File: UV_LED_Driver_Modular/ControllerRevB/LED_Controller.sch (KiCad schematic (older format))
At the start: 11 parts, among them J1 Barrel_Jack, J2 Conn_01x05, J4 Conn_02x04_Odd_Even, SW1 SW_SPST, SW3 SW_SPST, U1 STM32F051K8Tx, U2 L78L33_SOT89

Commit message: hw update
controller revb
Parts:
- added BZ1: Buzzer, Connector_PinHeader_2.54mm:PinHeader_1x02_P2.54mm_Vertical, symbol Device:Buzzer
- added D1: D, Diode_SMD:D_SOD-123F, symbol Device:D
- added Q1: MMBT3904, Package_TO_SOT_SMD:SOT-23, symbol Transistor_BJT:MMBT3904
- added SW4: SW_SPST, Connector_PinHeader_2.54mm:PinHeader_1x02_P2.54mm_Vertical, symbol Switch:SW_SPST
- added U3: MCP1416, Package_TO_SOT_SMD:SOT-23-5, symbol Driver_FET:MCP1416
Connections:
- net 3V3: now also SW4.1 (A)
- net GNDS: now also Q1.2 (E), U3.4 (GND)
- net VPP: now also BZ1.1 (-), D1.1 (K), U3.2 (Vdd)
- net BUZZER_PWM: now reaches U1.27 (PB4)
- net BUZZER_PWM: now also U3.3 (IN)
- net DOWN_BTN: now reaches U1.7 (PA1)
- net DOWN_BTN: now also SW4.2 (B)
- net MINUTE_BTN renamed UP_BTN
- new net: BZ1.2 (+), D1.2 (A), Q1.3 (C)
- new net: Q1.1 (B), U3.5 (OUT)
- no-connect marks 9 -> 7
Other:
- moved on the sheet: SW3
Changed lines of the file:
@@
 	-1   0    0    -1
 $EndComp
-Text Label 5325 2625 0    50   ~ 0
+Text Label 5200 2625 0    50   ~ 0
 NRST
 Wire Wire Line
-	5775 2625 5325 2625
+	5775 2625 5200 2625
 Wire Wire Line
 	4625 2825 4625 2975
@@
 	6475 2325 6475 2425
 Connection ~ 6375 2325
-Text Label 5275 3225 0    50   ~ 0
+Text Label 5175 3225 0    50   ~ 0
 ENABLE_LED
 Wire Wire Line
-	5275 3225 5775 3225
+	5175 3225 5775 3225
 Text Label 7625 3725 2    50   ~ 0
 LED_CTRL1
@@
 NoConn ~ 5775 4025
 NoConn ~ 5775 3925
-NoConn ~ 5775 3825
 NoConn ~ 5775 3325
 Text HLabel 9850 3250 2    50   Input ~ 0
@@
 	3150 5375 2650 5375
 Wire Wire Line
-	5775 3625 5275 3625
-Text Label 5275 3625 0    50   ~ 0
+	5775 3625 5175 3625
+Text Label 5175 3625 0    50   ~ 0
 LED_CTRL5
 Wire Wire Line
@@
 	6875 4125 7375 4125
 Wire Wire Line
-	5775 3725 5275 3725
-Text Label 5275 3725 0    50   ~ 0
+	5775 3725 5175 3725
+Text Label 5175 3725 0    50   ~ 0
 ENC_A
 Text Label 7375 4125 2    50   ~ 0
@@
 TFT_MOSI
 Wire Wire Line
-	5775 3525 5275 3525
-Text Label 5275 3525 0    50   ~ 0
+	5775 3525 5175 3525
+Text Label 5175 3525 0    50   ~ 0
 TFT_RST
 Wire Wire Line
@@
 Wire Wire Line
 	9800 1975 10250 1975
-NoConn ~ 6875 2725
 Text Label 8825 1975 0    50   ~ 0
 TFT_LED
@@
 L Switch:SW_SPST SW3
 U 1 1 5EFC8DE0
-P 2475 4150
-F 0 "SW3" H 2475 4385 50  0000 C CNN
-F 1 "SW_SPST" H 2475 4294 50  0000 C CNN
-F 2 "Connector_PinHeader_2.54mm:PinHeader_1x02_P2.54mm_Vertical" H 2475 4150 50  0001 C CNN
-F 3 "~" H 2475 4150 50  0001 C CNN
-	1    2475 4150
-	1    0    0    -1
-$EndComp
-Text Label 3175 4150 2    50   ~ 0
-MINUTE_BTN
-Wire Wire Line
-	3175 4150 2675 4150
+P 2450 3875
+F 0 "SW3" H 2450 4110 50  0000 C CNN
+F 1 "SW_SPST" H 2450 4019 50  0000 C CNN
+F 2 "Connector_PinHeader_2.54mm:PinHeader_1x02_P2.54mm_Vertical" H 2450 3875 50  0001 C CNN
+F 3 "~" H 2450 3875 50  0001 C CNN
+	1    2450 3875
+	1    0    0    -1
+$EndComp
+Text Label 3150 3875 2    50   ~ 0
+UP_BTN
+Wire Wire Line
+	3150 3875 2650 3875
 Text Label 7625 2825 2    50   ~ 0
-MINUTE_BTN
+UP_BTN
 Wire Wire Line
 	7625 2825 6875 2825
 Wire Wire Line
-	1875 4150 1875 3825
-Text HLabel 1875 3825 1    50   Input ~ 0
-3V3
-Wire Wire Line
-	1875 4150 2275 4150
+	1850 3875 1850 3550
+Text HLabel 1850 3550 1    50   Input ~ 0
+3V3
+Wire Wire Line
+	1850 3875 2250 3875
 Wire Wire Line
 	1850 5375 1850 5050
@@
 Text HLabel 10250 1975 2    50   Input ~ 0
 VPP
+$Comp
+L Device:Buzzer BZ1
+U 1 1 5EF2925A
+P 9400 4875
+F 0 "BZ1" H 9552 4904 50  0000 L CNN
+F 1 "Buzzer" H 9552 4813 50  0000 L CNN
+F 2 "Connector_PinHeader_2.54mm:PinHeader_1x02_P2.54mm_Vertical" V 9375 4975 50  0001 C CNN
+F 3 "~" V 9375 4975 50  0001 C CNN
+	1    9400 4875
+	1    0    0    -1
+$EndComp
+$Comp
+L Driver_FET:MCP1416 U3
+U 1 1 5EF2A524
+P 8200 5425
+F 0 "U3" H 7750 5825 50  0000 L CNN
+F 1 "MCP1416" H 7700 5725 50  0000 L CNN
+F 2 "Package_TO_SOT_SMD:SOT-23-5" H 8200 5025 50  0001 C CIN
+F 3 "http://ww1.microchip.com/downloads/en/DeviceDoc/20002092F.pdf" H 8000 5675 50  0001 C CNN
+	1    8200 5425
+	1    0    0    -1
+$EndComp
+$Comp
+L Transistor_BJT:MMBT3904 Q1
+U 1 1 5EF2B431
+P 9200 5425
+F 0 "Q1" H 9391 5471 50  0000 L CNN
+F 1 "MMBT3904" H 9391 5380 50  0000 L CNN
+F 2 "Package_TO_SOT_SMD:SOT-23" H 9400 5350 50  0001 L CIN
+F 3 "https://www.fairchildsemi.com/datasheets/2N/2N3904.pdf" H 9200 5425 50  0001 L CNN
+	1    9200 5425
+	1    0    0    -1
+$EndComp
+Text HLabel 8200 5000 1    50   Input ~ 0
+VPP
+Wire Wire Line
+	8200 5000 8200 5125
+$Comp
+L power:GNDS #PWR05
+U 1 1 5EF3198B
+P 8200 5925
+F 0 "#PWR05" H 8200 5675 50  0001 C CNN
+F 1 "GNDS" H 8205 5752 50  0000 C CNN
+F 2 "" H 8200 5925 50  0001 C CNN
+F 3 "" H 8200 5925 50  0001 C CNN
+	1    8200 5925
+	-1   0    0    -1
+$EndComp
+Wire Wire Line
+	8200 5925 8200 5725
+Wire Wire Line
+	8600 5425 9000 5425
+Text HLabel 9300 4400 1    50   Input ~ 0
+VPP
+Wire Wire Line
+	9300 4400 9300 4600
+$Comp
+L power:GNDS #PWR06
+U 1 1 5EF46BCB
+P 9300 5925
+F 0 "#PWR06" H 9300 5675 50  0001 C CNN
+F 1 "GNDS" H 9305 5752 50  0000 C CNN
+F 2 "" H 9300 5925 50  0001 C CNN
+F 3 "" H 9300 5925 50  0001 C CNN
+	1    9300 5925
+	-1   0    0    -1
+$EndComp
+Wire Wire Line
+	9300 5925 9300 5625
+Wire Wire Line
+	9300 4975 9300 5150
+$Comp
+L Device:D D1
+U 1 1 5EF4FFE8
+P 9000 4875
+F 0 "D1" V 8950 4725 50  0000 L CNN
+F 1 "D" V 9050 4725 50  0000 L CNN
+F 2 "Diode_SMD:D_SOD-123F" H 9000 4875 50  0001 C CNN
+F 3 "~" H 9000 4875 50  0001 C CNN
+	1    9000 4875
+	0    1    1    0
+$EndComp
+Wire Wire Line
+	9000 4725 9000 4600
+Wire Wire Line
+	9000 4600 9300 4600
+Connection ~ 9300 4600
+Wire Wire Line
+	9300 4600 9300 4775
+Wire Wire Line
+	9000 5025 9000 5150
+Wire Wire Line
+	9000 5150 9300 5150
+Connection ~ 9300 5150
+Wire Wire Line
+	9300 5150 9300 5225
+Wire Wire Line
+	5775 3825 5175 3825
+Text Label 5175 3825 0    50   ~ 0
+BUZZER_PWM
+Text Label 7250 5425 0    50   ~ 0
+BUZZER_PWM
+Wire Wire Line
+	7250 5425 7900 5425
+$Comp
+L Switch:SW_SPST SW4
+U 1 1 5EF795B5
+P 2450 4550
+F 0 "SW4" H 2450 4785 50  0000 C CNN
+F 1 "SW_SPST" H 2450 4694 50  0000 C CNN
+F 2 "Connector_PinHeader_2.54mm:PinHeader_1x02_P2.54mm_Vertical" H 2450 4550 50  0001 C CNN
+F 3 "~" H 2450 4550 50  0001 C CNN
+	1    2450 4550
+	1    0    0    -1
+$EndComp
+Text Label 3150 4550 2    50   ~ 0
+DOWN_BTN
+Wire Wire Line
+	3150 4550 2650 4550
+Wire Wire Line
+	1850 4550 1850 4225
+Text HLabel 1850 4225 1    50   Input ~ 0
+3V3
+Wire Wire Line
+	1850 4550 2250 4550
+Text Label 7625 2725 2    50   ~ 0
+DOWN_BTN
+Wire Wire Line
+	7625 2725 6875 2725
 $EndSCHEMATC

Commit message: updated
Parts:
- J1: footprint Connector_Molex:Molex_KK-396_A-41791-0002_1x02_P3.96mm_Vertical -> Connector_Molex:Molex_KK-254_AE-6410-02A_1x02_P2.54mm_Vertical
- R1: value 10K -> 1K
- R4: value 0R -> 1K
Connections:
- net 3V3: no longer R1.1
- net BUZZER_PWM: now also R1.2; no longer U3.3 (IN)
- net GNDS: now also U1.31 (BOOT0); no longer R4.2
- net at U3.5 (OUT): now also R4.2; no longer Q1.1 (B)
- new net: R1.1, U3.3 (IN)
- new net: Q1.1 (B), R4.1
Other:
- moved on the sheet: BZ1, D1, Q1, U3
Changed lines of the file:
@@
 Wire Wire Line
 	5775 2625 5200 2625
-Wire Wire Line
-	4625 2825 4625 2975
 $Comp
 L power:GNDS #PWR021
@@
 F 0 "J1" H 1682 1775 50  0000 C CNN
 F 1 "Barrel_Jack" H 1682 1684 50  0000 C CNN
-F 2 "Connector_Molex:Molex_KK-396_A-41791-0002_1x02_P3.96mm_Vertical" H 1675 1410 50  0001 C CNN
+F 2 "Connector_Molex:Molex_KK-254_AE-6410-02A_1x02_P2.54mm_Vertical" H 1675 1410 50  0001 C CNN
 F 3 "~" H 1675 1410 50  0001 C CNN
 	1    1625 1450
@@
 Wire Wire Line
 	9300 1875 8825 1875
-$Comp
-L Device:R R1
-U 1 1 5EF88471
-P 4625 2425
-F 0 "R1" H 4695 2471 50  0000 L CNN
-F 1 "10K" H 4695 2380 50  0000 L CNN
-F 2 "Resistor_SMD:R_1206_3216Metric_Pad1.42x1.75mm_HandSolder" V 4555 2425 50  0001 C CNN
-F 3 "~" H 4625 2425 50  0001 C CNN
-	1    4625 2425
-	1    0    0    -1
-$EndComp
-Wire Wire Line
-	4625 2575 4625 2825
-Connection ~ 4625 2825
-$Comp
-L Device:R R4
-U 1 1 5EF8AB44
-P 4625 3125
-F 0 "R4" H 4695 3171 50  0000 L CNN
-F 1 "0R" H 4695 3080 50  0000 L CNN
-F 2 "Resistor_SMD:R_1206_3216Metric_Pad1.42x1.75mm_HandSolder" V 4555 3125 50  0001 C CNN
-F 3 "~" H 4625 3125 50  0001 C CNN
-	1    4625 3125
-	1    0    0    -1
-$EndComp
-Wire Wire Line
-	4625 3275 4625 3500
 Wire Wire Line
 	4625 2825 5775 2825
-Wire Wire Line
-	4625 2275 4625 1800
-Text HLabel 4625 1800 1    50   Input ~ 0
-3V3
 $Comp
 L Switch:SW_SPST SW3
@@
 L Device:Buzzer BZ1
 U 1 1 5EF2925A
-P 9400 4875
-F 0 "BZ1" H 9552 4904 50  0000 L CNN
-F 1 "Buzzer" H 9552 4813 50  0000 L CNN
-F 2 "Connector_PinHeader_2.54mm:PinHeader_1x02_P2.54mm_Vertical" V 9375 4975 50  0001 C CNN
-F 3 "~" V 9375 4975 50  0001 C CNN
-	1    9400 4875
+P 10300 4750
+F 0 "BZ1" H 10452 4779 50  0000 L CNN
+F 1 "Buzzer" H 10452 4688 50  0000 L CNN
+F 2 "Connector_PinHeader_2.54mm:PinHeader_1x02_P2.54mm_Vertical" V 10275 4850 50  0001 C CNN
+F 3 "~" V 10275 4850 50  0001 C CNN
+	1    10300 4750
 	1    0    0    -1
 $EndComp
@@
 L Driver_FET:MCP1416 U3
 U 1 1 5EF2A524
-P 8200 5425
-F 0 "U3" H 7750 5825 50  0000 L CNN
-F 1 "MCP1416" H 7700 5725 50  0000 L CNN
-F 2 "Package_TO_SOT_SMD:SOT-23-5" H 8200 5025 50  0001 C CIN
-F 3 "http://ww1.microchip.com/downloads/en/DeviceDoc/20002092F.pdf" H 8000 5675 50  0001 C CNN
-	1    8200 5425
+P 8800 5300
+F 0 "U3" H 8350 5700 50  0000 L CNN
+F 1 "MCP1416" H 8300 5600 50  0000 L CNN
+F 2 "Package_TO_SOT_SMD:SOT-23-5" H 8800 4900 50  0001 C CIN
+F 3 "http://ww1.microchip.com/downloads/en/DeviceDoc/20002092F.pdf" H 8600 5550 50  0001 C CNN
+	1    8800 5300
 	1    0    0    -1
 $EndComp
@@
 L Transistor_BJT:MMBT3904 Q1
 U 1 1 5EF2B431
-P 9200 5425
-F 0 "Q1" H 9391 5471 50  0000 L CNN
-F 1 "MMBT3904" H 9391 5380 50  0000 L CNN
-F 2 "Package_TO_SOT_SMD:SOT-23" H 9400 5350 50  0001 L CIN
-F 3 "https://www.fairchildsemi.com/datasheets/2N/2N3904.pdf" H 9200 5425 50  0001 L CNN
-	1    9200 5425
-	1    0    0    -1
-$EndComp
-Text HLabel 8200 5000 1    50   Input ~ 0
+P 10100 5300
+F 0 "Q1" H 10291 5346 50  0000 L CNN
+F 1 "MMBT3904" H 10291 5255 50  0000 L CNN
+F 2 "Package_TO_SOT_SMD:SOT-23" H 10300 5225 50  0001 L CIN
+F 3 "https://www.fairchildsemi.com/datasheets/2N/2N3904.pdf" H 10100 5300 50  0001 L CNN
+	1    10100 5300
+	1    0    0    -1
+$EndComp
+Text HLabel 8800 4875 1    50   Input ~ 0
 VPP
 Wire Wire Line
-	8200 5000 8200 5125
+	8800 4875 8800 5000
 $Comp
 L power:GNDS #PWR05
 U 1 1 5EF3198B
-P 8200 5925
-F 0 "#PWR05" H 8200 5675 50  0001 C CNN
-F 1 "GNDS" H 8205 5752 50  0000 C CNN
-F 2 "" H 8200 5925 50  0001 C CNN
-F 3 "" H 8200 5925 50  0001 C CNN
-	1    8200 5925
+P 8800 5800
+F 0 "#PWR05" H 8800 5550 50  0001 C CNN
+F 1 "GNDS" H 8805 5627 50  0000 C CNN
+F 2 "" H 8800 5800 50  0001 C CNN
+F 3 "" H 8800 5800 50  0001 C CNN
+	1    8800 5800
 	-1   0    0    -1
 $EndComp
 Wire Wire Line
-	8200 5925 8200 5725
-Wire Wire Line
-	8600 5425 9000 5425
-Text HLabel 9300 4400 1    50   Input ~ 0
+	8800 5800 8800 5600
+Wire Wire Line
+	9200 5300 9425 5300
+Text HLabel 10200 4275 1    50   Input ~ 0
 VPP
 Wire Wire Line
-	9300 4400 9300 4600
+	10200 4275 10200 4475
 $Comp
 L power:GNDS #PWR06
 U 1 1 5EF46BCB
-P 9300 5925
-F 0 "#PWR06" H 9300 5675 50  0001 C CNN
-F 1 "GNDS" H 9305 5752 50  0000 C CNN
-F 2 "" H 9300 5925 50  0001 C CNN
-F 3 "" H 9300 5925 50  0001 C CNN
-	1    9300 5925
+P 10200 5800
+F 0 "#PWR06" H 10200 5550 50  0001 C CNN
+F 1 "GNDS" H 10205 5627 50  0000 C CNN
+F 2 "" H 10200 5800 50  0001 C CNN
+F 3 "" H 10200 5800 50  0001 C CNN
+	1    10200 5800
 	-1   0    0    -1
 $EndComp
 Wire Wire Line
-	9300 5925 9300 5625
-Wire Wire Line
-	9300 4975 9300 5150
+	10200 5800 10200 5500
+Wire Wire Line
+	10200 4850 10200 5025
 $Comp
 L Device:D D1
 U 1 1 5EF4FFE8
-P 9000 4875
-F 0 "D1" V 8950 4725 50  0000 L CNN
-F 1 "D" V 9050 4725 50  0000 L CNN
-F 2 "Diode_SMD:D_SOD-123F" H 9000 4875 50  0001 C CNN
-F 3 "~" H 9000 4875 50  0001 C CNN
-	1    9000 4875
+P 9900 4750
+F 0 "D1" V 9850 4600 50  0000 L CNN
+F 1 "D" V 9950 4600 50  0000 L CNN
+F 2 "Diode_SMD:D_SOD-123F" H 9900 4750 50  0001 C CNN
+F 3 "~" H 9900 4750 50  0001 C CNN
+	1    9900 4750
 	0    1    1    0
 $EndComp
 Wire Wire Line
-	9000 4725 9000 4600
-Wire Wire Line
-	9000 4600 9300 4600
-Connection ~ 9300 4600
-Wire Wire Line
-	9300 4600 9300 4775
-Wire Wire Line
-	9000 5025 9000 5150
-Wire Wire Line
-	9000 5150 9300 5150
-Connection ~ 9300 5150
-Wire Wire Line
-	9300 5150 9300 5225
+	9900 4600 9900 4475
+Wire Wire Line
+	9900 4475 10200 4475
+Connection ~ 10200 4475
+Wire Wire Line
+	10200 4475 10200 4650
+Wire Wire Line
+	9900 4900 9900 5025
+Wire Wire Line
+	9900 5025 10200 5025
+Connection ~ 10200 5025
+Wire Wire Line
+	10200 5025 10200 5100
 Wire Wire Line
 	5775 3825 5175 3825
 Text Label 5175 3825 0    50   ~ 0
 BUZZER_PWM
-Text Label 7250 5425 0    50   ~ 0
+Text Label 7350 5300 0    50   ~ 0
 BUZZER_PWM
 Wire Wire Line
-	7250 5425 7900 5425
+	7350 5300 8000 5300
 $Comp
 L Switch:SW_SPST SW4
@@
 Wire Wire Line
 	7625 2725 6875 2725
+Wire Wire Line
+	4625 2825 4625 3500
+$Comp
+L Device:R R1
+U 1 1 5EF88709
+P 8150 5300
+F 0 "R1" V 7943 5300 50  0000 C CNN
+F 1 "1K" V 8034 5300 50  0000 C CNN
+F 2 "Resistor_SMD:R_1206_3216Metric_Pad1.42x1.75mm_HandSolder" V 8080 5300 50  0001 C CNN
+F 3 "~" H 8150 5300 50  0001 C CNN
+	1    8150 5300
+	0    1    1    0
+$EndComp
+Wire Wire Line
+	8300 5300 8500 5300
+$Comp
+L Device:R R4
+U 1 1 5EF94EF7
+P 9575 5300
+F 0 "R4" V 9368 5300 50  0000 C CNN
+F 1 "1K" V 9459 5300 50  0000 C CNN
+F 2 "Resistor_SMD:R_1206_3216Metric_Pad1.42x1.75mm_HandSolder" V 9505 5300 50  0001 C CNN
+F 3 "~" H 9575 5300 50  0001 C CNN
+	1    9575 5300
+	0    1    1    0
+$EndComp
+Wire Wire Line
+	9725 5300 9900 5300
 $EndSCHEMATC

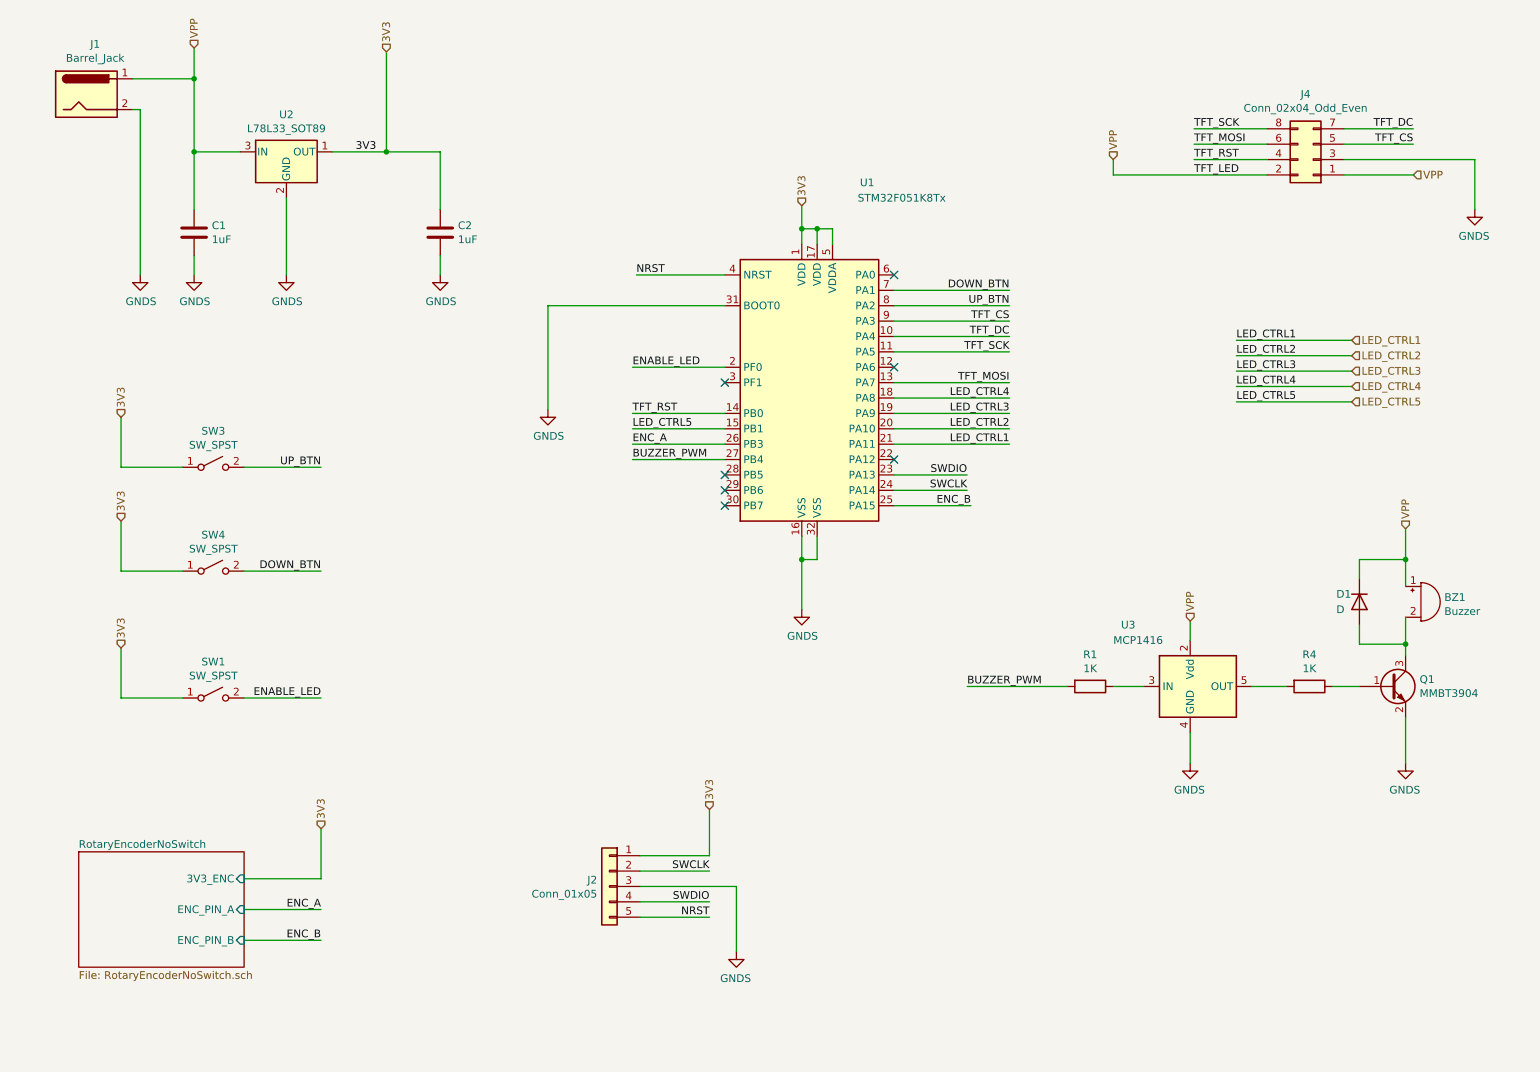
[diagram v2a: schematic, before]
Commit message: Updated prototype designs for fab
updated readme
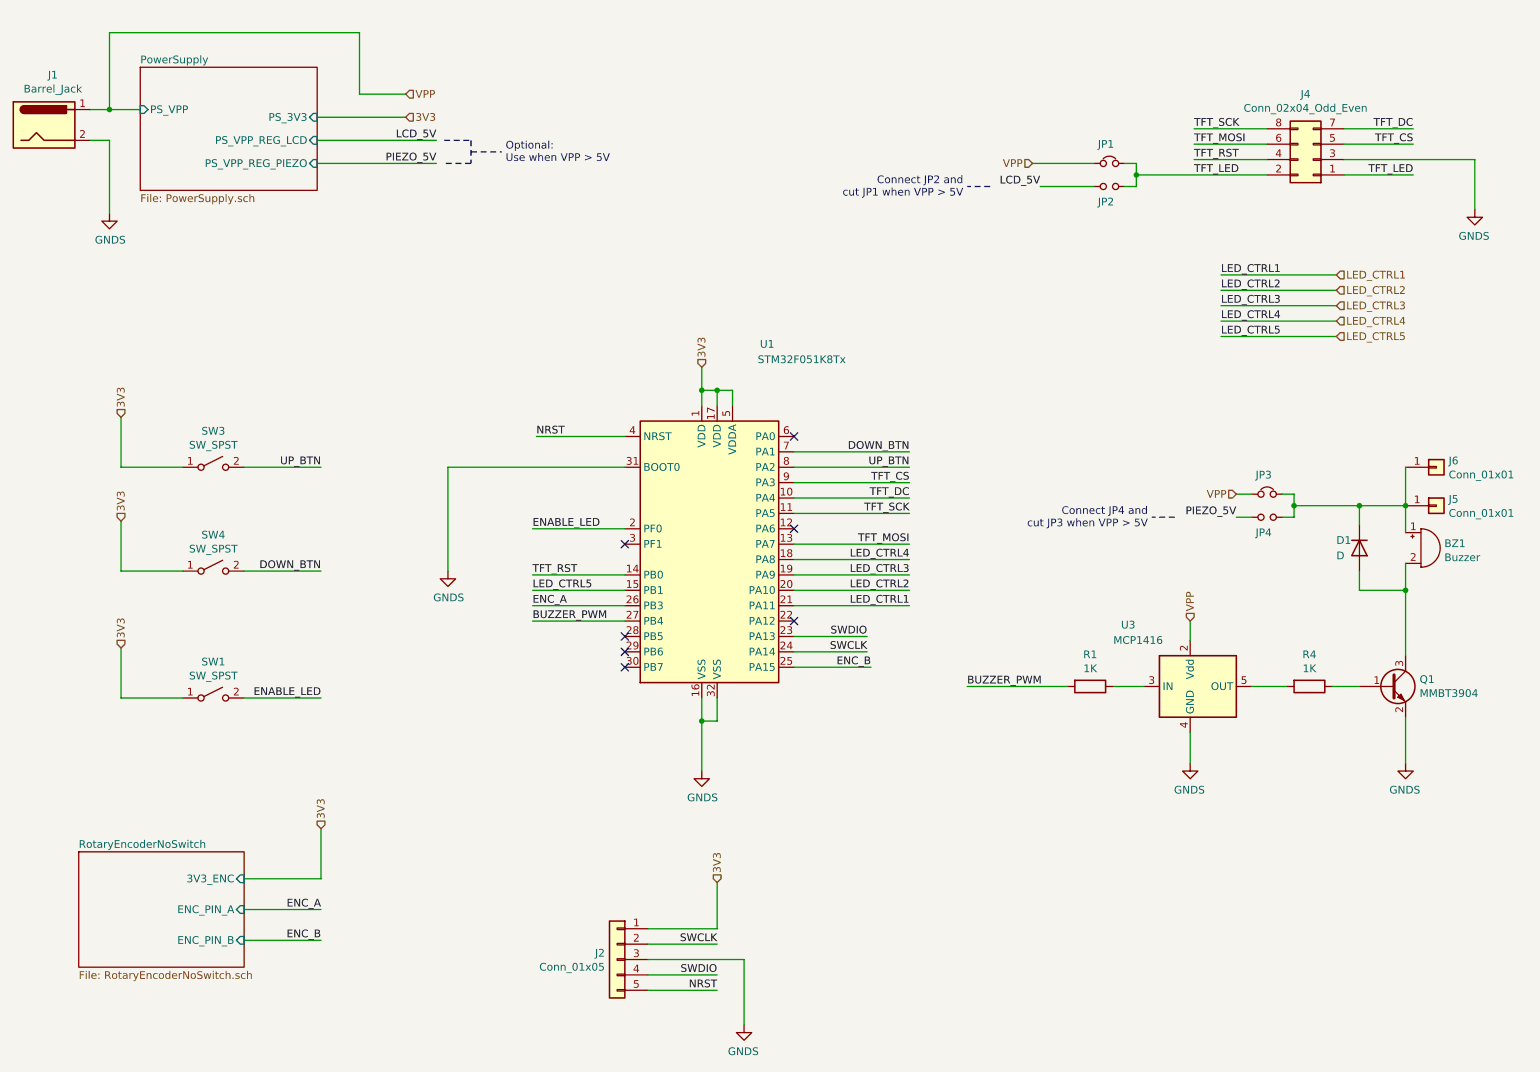
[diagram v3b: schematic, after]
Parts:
- removed C1, C2: 1uF, Capacitor_SMD:C_1206_3216Metric_Pad1.42x1.75mm_HandSolder, symbol Device:C
- removed U2: L78L33_SOT89, Package_TO_SOT_SMD:SOT-89-3, symbol Regulator_Linear:L78L33_SOT89
- added J5, J6: Conn_01x01, Connector_PinHeader_2.54mm:PinHeader_1x01_P2.54mm_Vertical, symbol Connector_Generic:Conn_01x01
- added JP1, JP3: Jumper_NC_Small, Jumper:SolderJumper-2_P1.3mm_Bridged_Pad1.0x1.5mm, symbol Device:Jumper_NC_Small
- added JP2, JP4: Jumper_NO_Small, Jumper:SolderJumper-2_P1.3mm_Open_Pad1.0x1.5mm, symbol Device:Jumper_NO_Small
- BZ1: footprint Connector_PinHeader_2.54mm:PinHeader_1x02_P2.54mm_Vertical -> Buzzer_Beeper:Buzzer_12x9.5RM7.6
- R1, R4: footprint Resistor_SMD:R_1206_3216Metric_Pad1.42x1.75mm_HandSolder -> Resistor_SMD:R_0805_2012Metric_Pad1.15x1.40mm_HandSolder
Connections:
- net VPP: now also JP1.1, JP3.1; no longer BZ1.1 (-), D1.1 (K), J4.1 (Pin_1), J4.2 (Pin_2)
- new net: BZ1.1 (-), D1.1 (K), J5.1 (Pin_1), J6.1 (Pin_1), JP3.2, JP4.2
- new net LCD_5V: JP2.1
- new net PIEZO_5V: JP4.1
- new net TFT_LED: J4.1 (Pin_1), J4.2 (Pin_2), JP1.2, JP2.2
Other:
- note added: "Connect JP2 and \ncut JP1 when VPP > 5V"
- note added: "Connect JP4 and \ncut JP3 when VPP > 5V"
- note added: "Optional:\nUse when VPP > 5V"
- moved on the sheet: BZ1, D1, J2, U1
